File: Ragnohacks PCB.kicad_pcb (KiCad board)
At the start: 2 copper layers, 85.6 x 54 mm, 35 parts, among them J1 Conn_01x02, J2 Conn_01x18, J3 Conn_01x18, J4 USB_A, SW1 SW_Push, U1 RP2040, U2 W25Q128JVS, U3 LD1117S33TR_SOT223, U4 USBLC6-2P6, Y1 12MHz

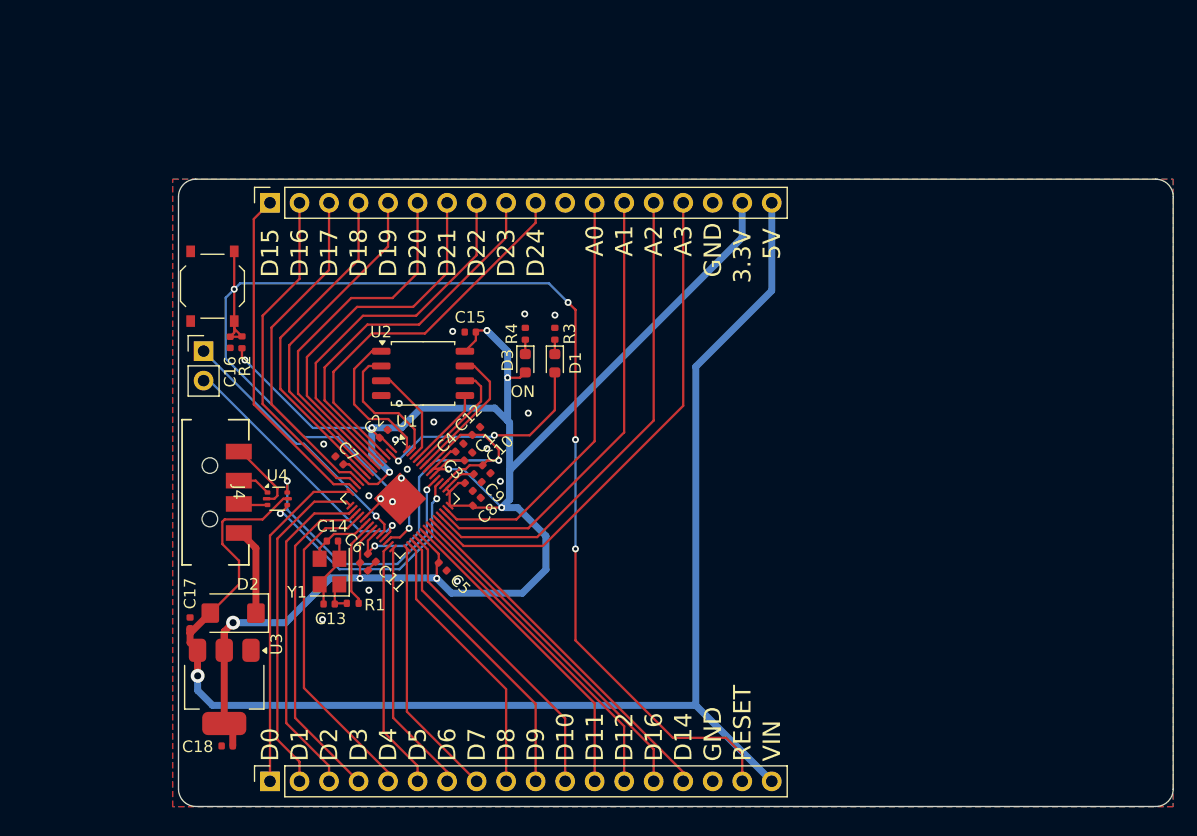
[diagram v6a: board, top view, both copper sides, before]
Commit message: Change USB port, adjust header position, start tracing
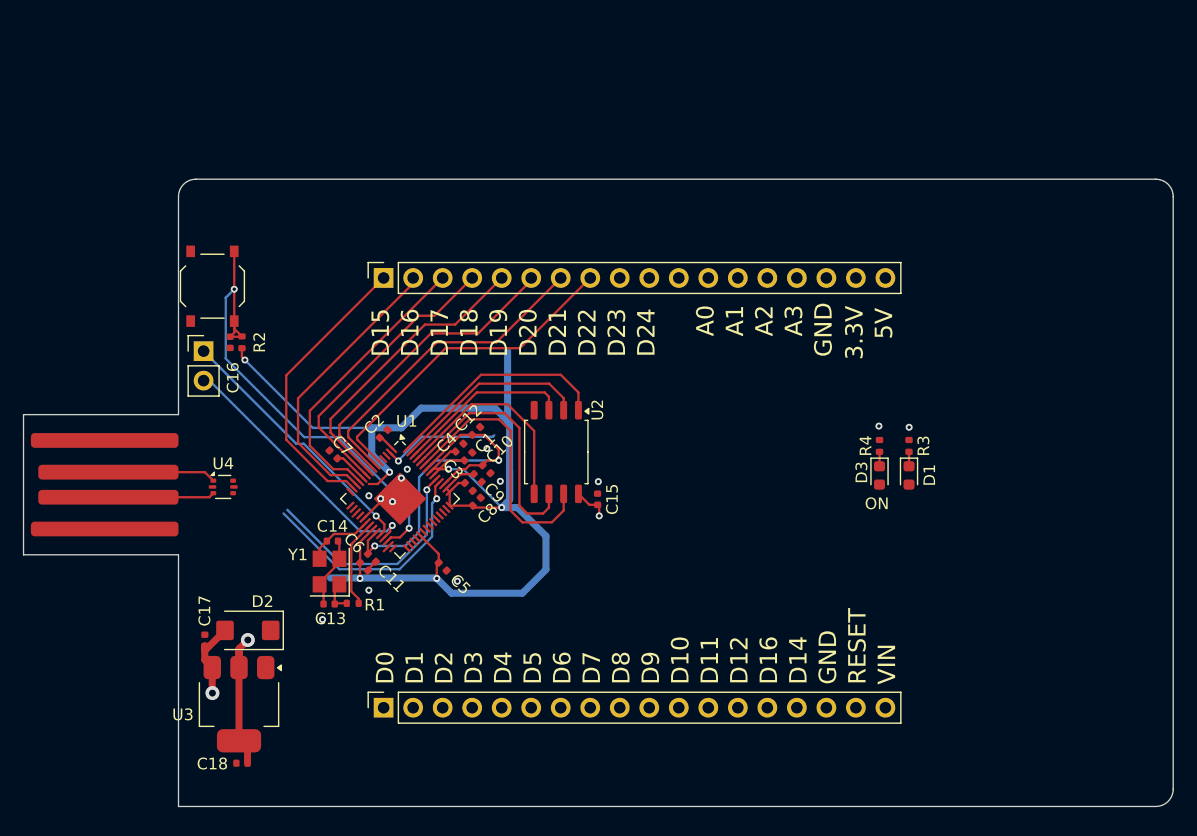
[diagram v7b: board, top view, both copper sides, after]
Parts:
- J4: footprint Connector_USB:USB_A_Keystone_931_Horizontal -> Connector_USB:USB_A_Onboard
- moved D1 32.0 mm to (166.4, 102.9)
- moved D3 32.0 mm to (163.8, 102.9)
- moved R3 32.0 mm to (166.4, 100.4)
- moved R4 32.0 mm to (163.8, 100.4)
- moved J4 21.1 mm to (97.5, 103.7), turned to 90 degrees
- moved C15 18.1 mm to (139.6, 104.9), turned to 90 degrees
- moved U2 13.3 mm to (136.0, 100.9), turned to -90 degrees
- moved J3 11.7 mm to (121.2, 85.9)
- moved J2 11.7 mm to (121.2, 122.9)
- moved U4 4.77 mm to (107.4, 103.9)
- moved D2 1.95 mm to (109.5, 116.2)
- moved U3 1.95 mm to (108.7, 122.6)
- moved C17 1.95 mm to (105.8, 117.1)
- moved C18 1.95 mm to (109.0, 127.7)
- moved C7 0.72 mm to (116.8, 101.1)
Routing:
- net +5V: track 123.0 -> 7.20 mm
- net RESET: track 123.1 -> 41.6 mm, vias 5 -> 2
- net +3V3: track 178.9 -> 132.3 mm, vias 10 -> 8
- net A3: track 44.7 -> 0.00 mm
- net A2: track 42.1 -> 0.00 mm
- net A1: track 39.3 -> 0.00 mm
- net A0: track 36.4 -> 0.00 mm
- net D24: track 33.5 -> 0.00 mm
- net D23: track 33.2 -> 0.00 mm
- net D14: track 31.2 -> 0.00 mm
- net D13: track 30.0 -> 0.00 mm
- net D0: track 29.6 -> 0.00 mm
- net D1: track 29.4 -> 0.00 mm
- net D2: track 29.1 -> 0.00 mm
- net D3: track 29.0 -> 0.00 mm
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- removed copper zone on B.Cu, net GND
- removed copper zone on F.Cu, net GND
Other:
- outline, holes or cut-outs redrawn

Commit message: Rev 2 of the Ragnohacks PCB
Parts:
- added J5: USB_C_Receptacle_USB2.0_16P, Connector_USB:USB_C_Receptacle_GCT_USB4105-xx-A_16P_TopMnt_Horizontal, F.Cu at (123.2, 122.7)
- added R5: 5k1, Capacitor_SMD:C_0402_1005Metric, F.Cu at (126.6, 116.8)
- added R6: 5k1, Capacitor_SMD:C_0402_1005Metric, F.Cu at (128.8, 118.9)
- J4: footprint Connector_USB:USB_A_Onboard -> Connector_USB:USB_A_Edge
- moved SW1 82.4 mm to (181.1, 121.4), turned to -90 degrees
- moved J1 79.8 mm to (181.9, 115.9), turned to 180 degrees
- moved C18 79.5 mm to (179.1, 90.3), turned to 0 degrees
- moved C17 78.2 mm to (182.3, 100.8), turned to -90 degrees
- moved C16 75.9 mm to (179.6, 116.6), turned to -90 degrees
- moved U3 75.7 mm to (179.3, 95.4), turned to 90 degrees
- moved R2 74.0 mm to (178.6, 116.6), turned to 90 degrees
- moved J2 66.4 mm to (175.8, 85.2), turned to -90 degrees
- moved J3 65.5 mm to (175.8, 122.2), turned to -90 degrees
- moved C13 57.7 mm to (170.0, 92.4), turned to 180 degrees
- moved Y1 55.8 mm to (170.0, 95.2), turned to -90 degrees
- moved C14 54.1 mm to (169.7, 97.9), turned to 0 degrees
- moved R1 53.9 mm to (168.0, 92.5), turned to 180 degrees
- moved C7 53.0 mm to (169.7, 105.3), turned to -45 degrees
- moved C6 49.9 mm to (167.0, 95.7), turned to 135 degrees
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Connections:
- net Net-(J4-D+) renamed DN
- net Net-(J4-D-) renamed DP
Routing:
- net +5V: track 7.20 -> 129.9 mm, vias 1 -> 0
- net Net-(D2-A): track 0.00 -> 45.2 mm
- net A3: track 0.00 -> 45.0 mm
- net RESET: track 41.6 -> 86.1 mm, vias 2 -> 3
- net A2: track 0.00 -> 42.1 mm
- net A1: track 0.00 -> 40.9 mm
- net USB_DP: track 20.1 -> 60.9 mm, vias 1 -> 2
- net A0: track 0.00 -> 39.1 mm
- net USB_DN: track 21.0 -> 58.8 mm, vias 1 -> 2
- net +3V3: track 132.3 -> 169.1 mm, vias 8 -> 9
- net D14: track 0.00 -> 26.8 mm
- net D13: track 0.00 -> 24.4 mm
- net D0: track 0.00 -> 22.7 mm
- net D24: track 0.00 -> 22.4 mm
- net D23: track 0.00 -> 22.2 mm
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- added copper zone on B.Cu, net GND
- added copper zone on F.Cu, net GND
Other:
- outline, holes or cut-outs redrawn
